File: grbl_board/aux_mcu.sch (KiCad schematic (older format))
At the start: 54 parts, among them J17 USB_B, J18 ICSP, Q5 BSS127S, Q6 BSS127S, Q7 BSS127S, SW2 SW_Push, U25 FT231XS, U26 40106, U27 74LS155, U28 ATmega328P-AU, U29 74LS153, U30 74LS153, Y2 16M

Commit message: routing done
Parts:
- removed C35, C37: 100n, Capacitor_SMD:C_0603_1608Metric_Pad1.05x0.95mm_HandSolder, symbol Device:C
- removed R59, R60: 10k, Resistor_SMD:R_0805_2012Metric_Pad1.15x1.40mm_HandSolder, symbol Device:R
- J17: symbol grbl_board-rescue:USB_B-Connector -> Connector:USB_B
- renumbered C42 to C35, C38 to C37, C39 to C38, C40 to C39, C44 to C40, C43 to C42, C47 to C43, C45 to C44, C46 to C45, C48 to C46, D47 to D44, D48 to D45, D49 to D46, D50 to D47, D51 to D48
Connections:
- net X_EN: now also U26.6; no longer U26.2
- net Z_EN: now also U26.2; no longer U26.6
- net at U26.5: now also U27.9 (Q0b); no longer U27.11 (Q2b)
- net at U26.1: now also U27.11 (Q2b); no longer U27.9 (Q0b)
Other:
- moved on the sheet: C35, C40, C43, L5, U26A, U26C

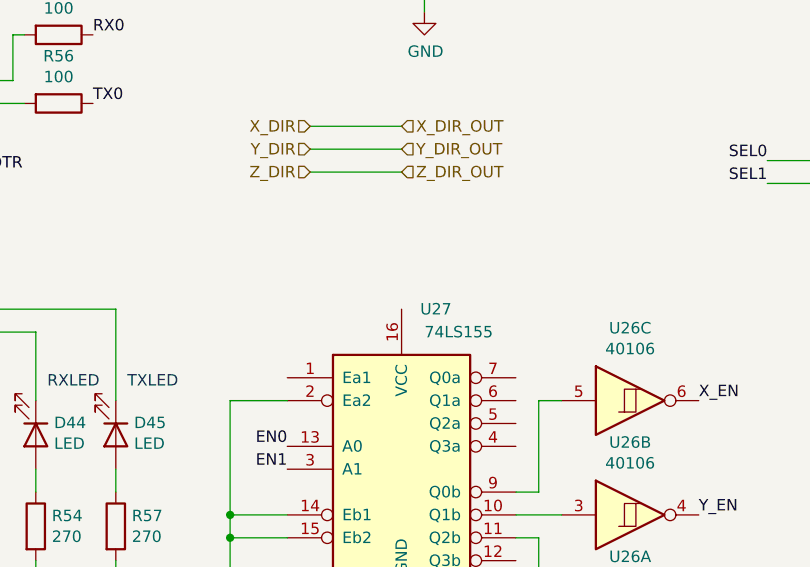
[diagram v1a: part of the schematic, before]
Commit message: added usb 3d model and fixed footprint associations
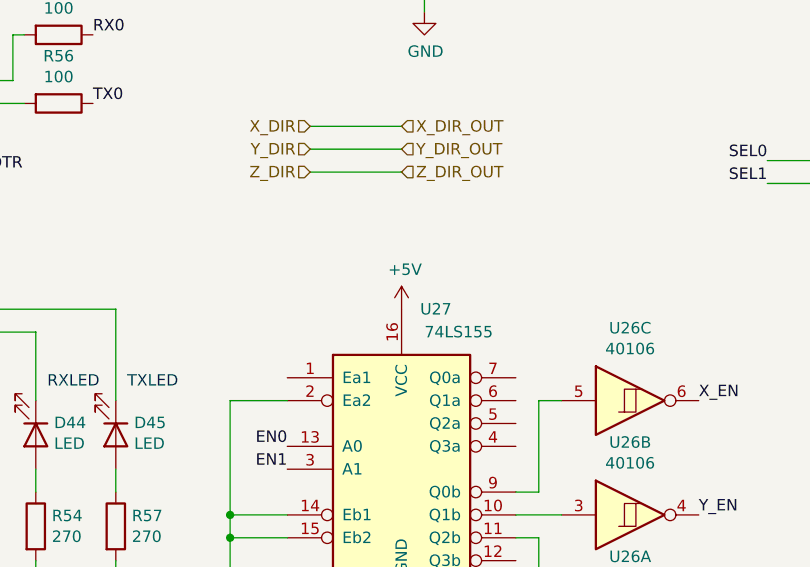
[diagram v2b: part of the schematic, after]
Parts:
- J17: footprint Connector_USB:USB_B_OST_USB-B1HSxx_Horizontal -> grbl_board:USB_B_OST_USB-B1HSxx_Horizontal
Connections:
- net +5V: now also U27.16 (VCC)
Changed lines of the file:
@@
 F 0 "J17" H 907 4367 50  0000 C CNN
 F 1 "USB_B" H 907 4276 50  0000 C CNN
-F 2 "Connector_USB:USB_B_OST_USB-B1HSxx_Horizontal" H 1000 3850 50  0001 C CNN
+F 2 "grbl_board:USB_B_OST_USB-B1HSxx_Horizontal" H 1000 3850 50  0001 C CNN
 F 3 "https://belfuse.com/resources/datasheets/stewartconnector/ds-stw-usb-2.0-type-b-connectors.pdf" H 1000 3850 50  0001 C CNN
 F 4 "380-1492-ND" H 850 3900 50  0001 C CNN "Digikey Part No."
@@
 Wire Wire Line
 	6800 5100 7850 5100
+$Comp
+L power:+5V #PWR0104
+U 1 1 62525187
+P 5200 5650
+F 0 "#PWR0104" H 5200 5500 50  0001 C CNN
+F 1 "+5V" H 5215 5823 50  0000 C CNN
+F 2 "" H 5200 5650 50  0001 C CNN
+F 3 "" H 5200 5650 50  0001 C CNN
+	1    5200 5650
+	1    0    0    -1
+$EndComp
 $EndSCHEMATC

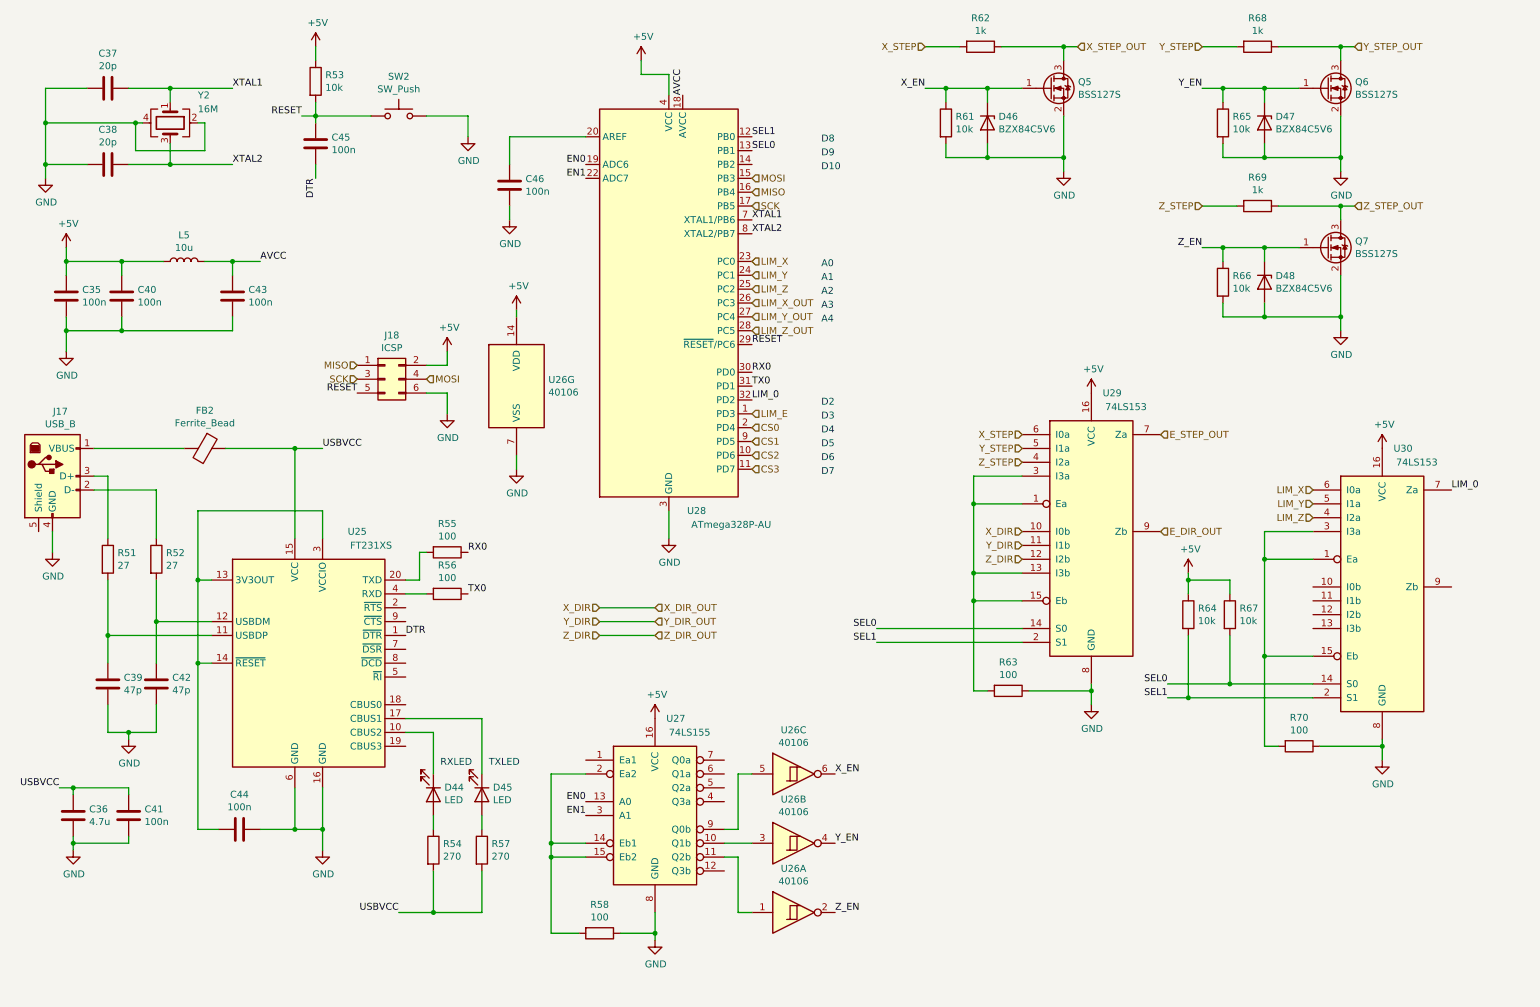
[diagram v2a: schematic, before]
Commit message: added some descriptions in the schematic and added gerber file
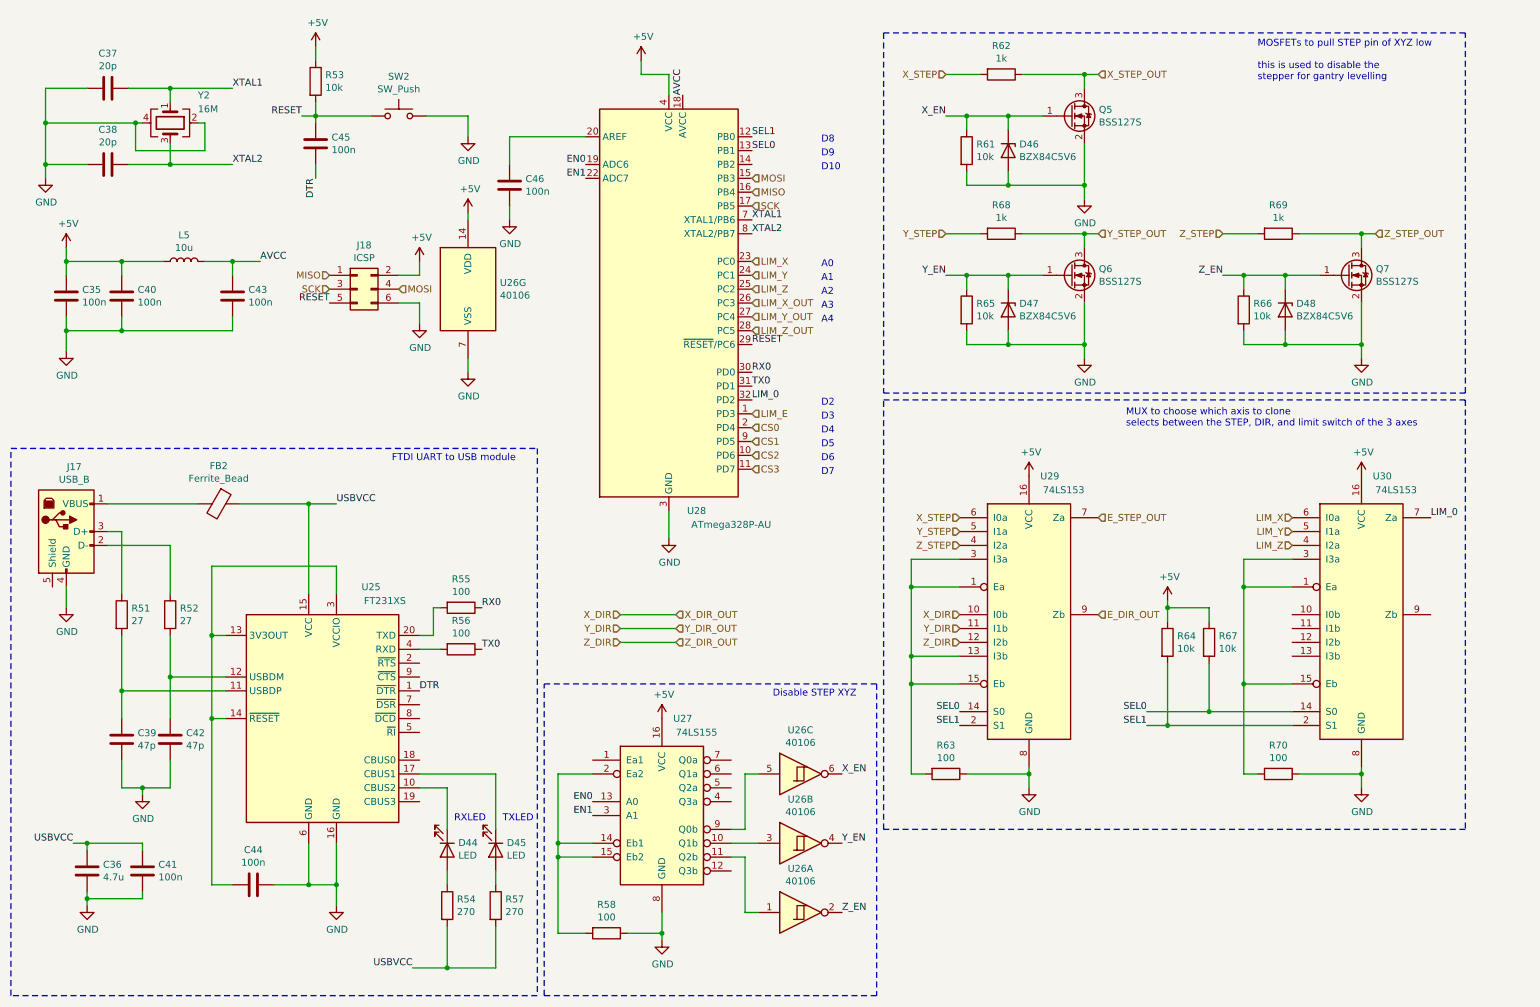
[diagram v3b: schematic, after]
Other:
- note added: "Disable STEP XYZ"
- note added: "FTDI UART to USB module\n"
- note added: "MOSFETs to pull STEP pin of XYZ low\n\nthis is used to disable the \nstepper for gantry levelling\n"
- note added: "MUX to choose which axis to clone\nselects between the STEP, DIR, and limit switch of the 3 axes"
- moved on the sheet: C36, C39, C41, C42, C44, D44, D45, D46, D47, D48, FB2, J17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
